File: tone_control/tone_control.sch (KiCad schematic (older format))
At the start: 17 parts, among them J1 filament, J2 B+, J3 audio_in, J4 earth, J5 bass pot (1M), J6 treble pot (250K), J7 audio_out

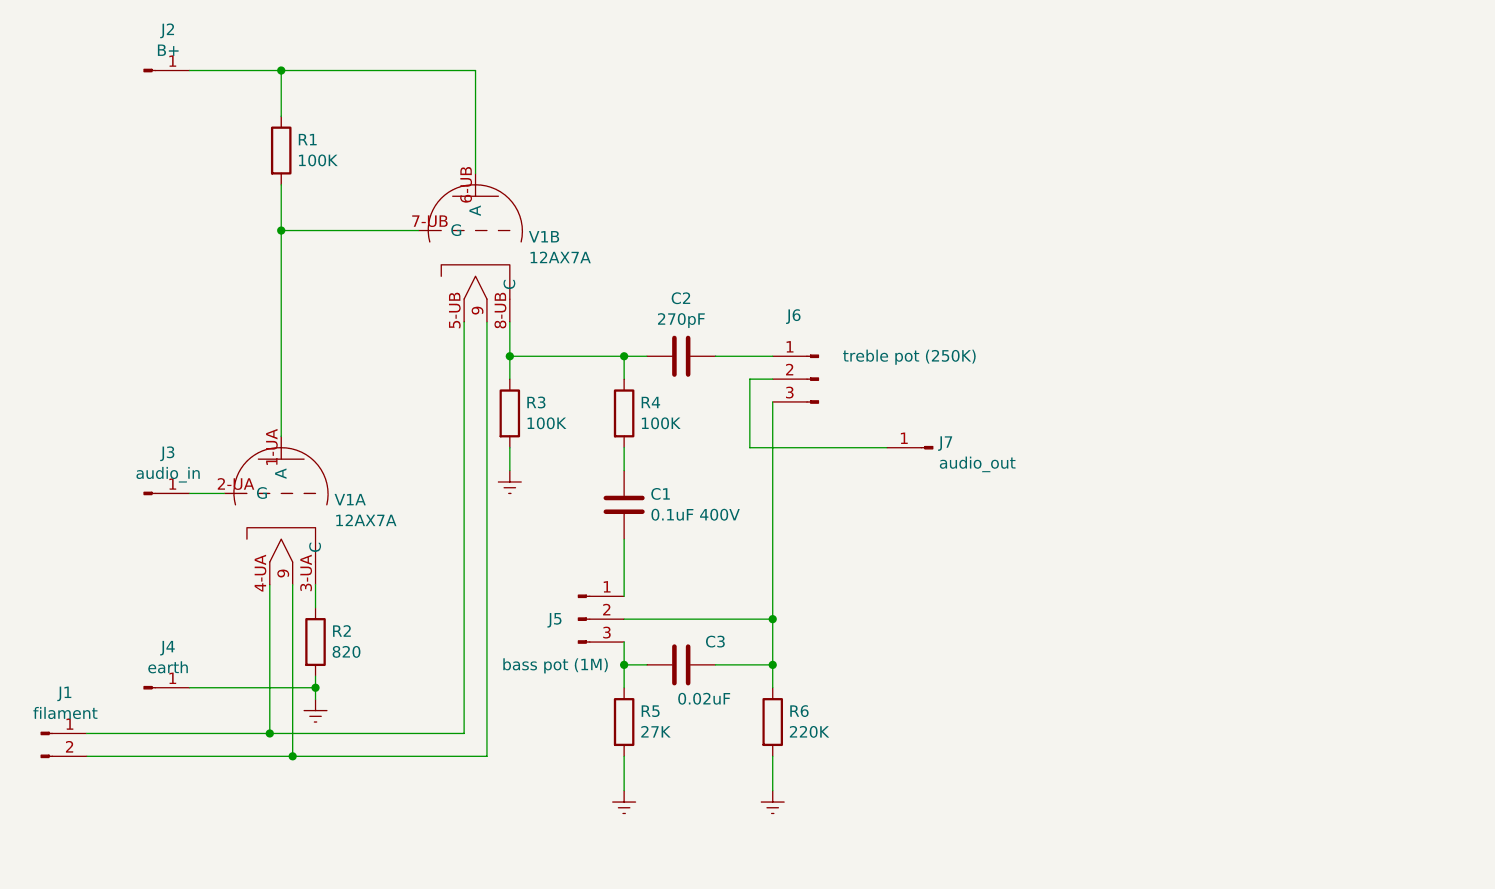
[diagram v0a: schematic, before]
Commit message: refine tone control schematic
some things are chassis mounted
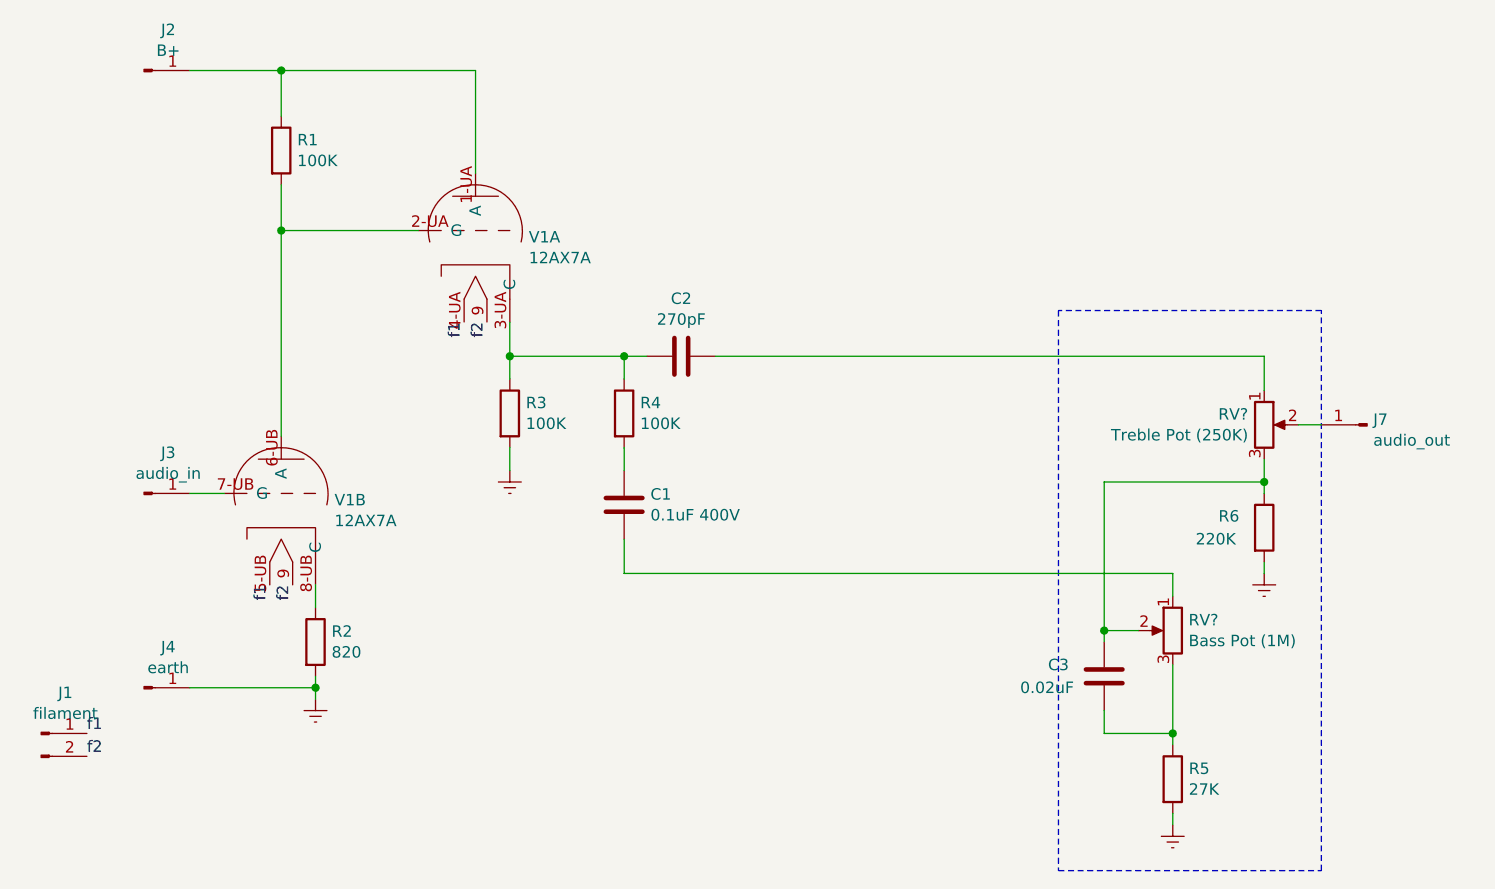
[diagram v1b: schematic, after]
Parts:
- removed J5: bass pot (1M), symbol Connector:Conn_01x03_Male
- removed J6: treble pot (250K), symbol Connector:Conn_01x03_Male
- added RV?: Treble Pot (250K), symbol Device:R_POT
- added RV?: Bass Pot (1M), symbol Device:R_POT
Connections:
- net at J3.1 (Pin_1): now also V1.7-UB (G); no longer V1.2-UA (G)
- net at V1.3-UA (C): now also C2.2, R3.1, R4.1; no longer R2.1
- net f1: now reaches J1.1 (Pin_1), V1.4-UA, V1.5-UB
- net f2: now reaches J1.2 (Pin_2), V1.9, V1.9
- net at J2.1 (Pin_1), R1.1: now also V1.1-UA (A); no longer V1.6-UB (A)
- net at C1.2: now also RV?.1
- net at C2.1: now also RV?.1
- net at J7.1 (Pin_1): now also RV?.2
- net at C3.1, R6.1: now also RV?.2, RV?.3
- net at C3.2, R5.1: now also RV?.3
- new net: R1.2, V1.2-UA (G), V1.6-UB (A)
- new net: R2.1, V1.8-UB (C)
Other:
- moved on the sheet: C3, J7, R5, R6, V1A, V1B
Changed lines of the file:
@@
 EESchema Schematic File Version 4
+LIBS:tone_control-cache
 EELAYER 26 0
 EELAYER END
@@
 L yga1:12AX7A V1
 U 1 1 5C54845C
+P 4900 2050
+F 0 "V1" H 5133 2271 50  0000 L CNN
+F 1 "12AX7A" H 5133 2180 50  0000 L CNN
+F 2 "" H 4900 1700 50  0001 C CNN
+F 3 "" H 4900 1700 50  0001 C CNN
+	1    4900 2050
+	1    0    0    -1
+$EndComp
+$Comp
+L yga1:12AX7A V1
+U 2 1 5C5484C9
 P 4050 3200
 F 0 "V1" H 4283 3421 50  0000 L CNN
@@
 F 2 "" H 4050 2850 50  0001 C CNN
 F 3 "" H 4050 2850 50  0001 C CNN
-	1    4050 3200
-	1    0    0    -1
-$EndComp
-$Comp
-L yga1:12AX7A V1
-U 2 1 5C5484C9
-P 4900 2050
-F 0 "V1" H 5133 2271 50  0000 L CNN
-F 1 "12AX7A" H 5133 2180 50  0000 L CNN
-F 2 "" H 4900 1700 50  0001 C CNN
-F 3 "" H 4900 1700 50  0001 C CNN
-	2    4900 2050
+	2    4050 3200
 	1    0    0    -1
 $EndComp
@@
 	1    0    0    -1
 $EndComp
-Wire Wire Line
-	4000 3350 4000 4000
-Wire Wire Line
-	4000 4000 3200 4000
-Wire Wire Line
-	4100 3350 4100 4100
-Wire Wire Line
-	4100 4100 3200 4100
-Wire Wire Line
-	4100 4100 4950 4100
-Wire Wire Line
-	4950 4100 4950 2200
-Connection ~ 4100 4100
-Wire Wire Line
-	4000 4000 4850 4000
-Wire Wire Line
-	4850 4000 4850 2200
-Connection ~ 4000 4000
 Wire Wire Line
 	4200 3450 4200 3350
@@
 Connection ~ 5550 2350
 $Comp
-L Connector:Conn_01x03_Male J6
-U 1 1 5C54A25B
-P 6400 2450
-F 0 "J6" H 6506 2728 50  0000 C CNN
-F 1 "treble pot (250K)" H 6000 2550 50  0000 C CNN
-F 2 "" H 6400 2450 50  0001 C CNN
-F 3 "~" H 6400 2450 50  0001 C CNN
-	1    6400 2450
-	-1   0    0    -1
-$EndComp
-Wire Wire Line
-	5950 2350 6200 2350
-$Comp
 L Connector:Conn_01x01_Male J7
 U 1 1 5C54A938
-P 6900 2750
-F 0 "J7" H 6873 2773 50  0000 R CNN
-F 1 "audio_out" H 6873 2682 50  0000 R CNN
-F 2 "" H 6900 2750 50  0001 C CNN
-F 3 "~" H 6900 2750 50  0001 C CNN
-	1    6900 2750
+P 8800 2650
+F 0 "J7" H 8773 2673 50  0000 R CNN
+F 1 "audio_out" H 8773 2582 50  0000 R CNN
+F 2 "" H 8800 2650 50  0001 C CNN
+F 3 "~" H 8800 2650 50  0001 C CNN
+	1    8800 2650
 	-1   0    0    -1
 $EndComp
-$Comp
-L Connector:Conn_01x03_Male J5
-U 1 1 5C54AA69
-P 5350 3500
-F 0 "J5" H 5250 3500 50  0000 C CNN
-F 1 "bass pot (1M)" H 5250 3300 50  0000 C CNN
-F 2 "" H 5350 3500 50  0001 C CNN
-F 3 "~" H 5350 3500 50  0001 C CNN
-	1    5350 3500
-	1    0    0    -1
-$EndComp
-Wire Wire Line
-	5550 3150 5550 3400
+Wire Wire Line
+	5550 3150 5550 3300
 $Comp
 L Device:R R5
 U 1 1 5C54AE63
-P 5550 3950
-F 0 "R5" H 5620 3996 50  0000 L CNN
-F 1 "27K" H 5620 3905 50  0000 L CNN
-F 2 "" V 5480 3950 50  0001 C CNN
-F 3 "~" H 5550 3950 50  0001 C CNN
-	1    5550 3950
-	1    0    0    -1
-$EndComp
-Wire Wire Line
-	5550 3600 5550 3700
-$Comp
-L power:Earth #PWR03
-U 1 1 5C54B1C4
-P 5550 4250
-F 0 "#PWR03" H 5550 4000 50  0001 C CNN
-F 1 "Earth" H 5550 4100 50  0001 C CNN
-F 2 "" H 5550 4250 50  0001 C CNN
-F 3 "~" H 5550 4250 50  0001 C CNN
-	1    5550 4250
-	1    0    0    -1
-$EndComp
-Wire Wire Line
-	5550 4100 5550 4250
+P 7950 4200
+F 0 "R5" H 8020 4246 50  0000 L CNN
+F 1 "27K" H 8020 4155 50  0000 L CNN
+F 2 "" V 7880 4200 50  0001 C CNN
+F 3 "~" H 7950 4200 50  0001 C CNN
+	1    7950 4200
+	1    0    0    -1
+$EndComp
 $Comp
 L Device:C C3
 U 1 1 5C54B510
-P 5800 3700
-F 0 "C3" V 5700 3850 50  0000 C CNN
-F 1 "0.02uF" V 5950 3800 50  0000 C CNN
-F 2 "" H 5838 3550 50  0001 C CNN
-F 3 "~" H 5800 3700 50  0001 C CNN
-	1    5800 3700
-	0    1    1    0
-$EndComp
-Wire Wire Line
-	5650 3700 5550 3700
-Connection ~ 5550 3700
-Wire Wire Line
-	5550 3700 5550 3800
-Wire Wire Line
-	6200 2550 6200 3500
-Wire Wire Line
-	6200 3500 5550 3500
-Wire Wire Line
-	6200 3500 6200 3700
-Wire Wire Line
-	6200 3700 5950 3700
-Connection ~ 6200 3500
+P 7650 3750
+F 0 "C3" H 7450 3800 50  0000 C CNN
+F 1 "0.02uF" H 7400 3700 50  0000 C CNN
+F 2 "" H 7688 3600 50  0001 C CNN
+F 3 "~" H 7650 3750 50  0001 C CNN
+	1    7650 3750
+	1    0    0    -1
+$EndComp
 $Comp
 L Device:R R6
 U 1 1 5C54C0D0
-P 6200 3950
-F 0 "R6" H 6270 3996 50  0000 L CNN
-F 1 "220K" H 6270 3905 50  0000 L CNN
-F 2 "" V 6130 3950 50  0001 C CNN
-F 3 "~" H 6200 3950 50  0001 C CNN
-	1    6200 3950
-	1    0    0    -1
-$EndComp
-$Comp
-L power:Earth #PWR04
-U 1 1 5C54C54E
-P 6200 4250
-F 0 "#PWR04" H 6200 4000 50  0001 C CNN
-F 1 "Earth" H 6200 4100 50  0001 C CNN
-F 2 "" H 6200 4250 50  0001 C CNN
-F 3 "~" H 6200 4250 50  0001 C CNN
-	1    6200 4250
-	1    0    0    -1
-$EndComp
-Wire Wire Line
-	6200 4100 6200 4250
-Wire Wire Line
-	6200 3700 6200 3800
-Connection ~ 6200 3700
-Wire Wire Line
-	6200 2450 6100 2450
-Wire Wire Line
-	6100 2450 6100 2750
-Wire Wire Line
-	6100 2750 6700 2750
+P 8350 3100
+F 0 "R6" H 8150 3150 50  0000 L CNN
+F 1 "220K" H 8050 3050 50  0000 L CNN
+F 2 "" V 8280 3100 50  0001 C CNN
+F 3 "~" H 8350 3100 50  0001 C CNN
+	1    8350 3100
+	1    0    0    -1
+$EndComp
 $Comp
 L Connector:Conn_01x01_Male J4
@@
 Wire Wire Line
 	4200 3800 4200 3850
+Text Label 3200 4000 0    50   ~ 0
+f1
+Text Label 3200 4100 0    50   ~ 0
+f2
+Text Label 4850 2200 3    50   ~ 0
+f1
+Text Label 4950 2200 3    50   ~ 0
+f2
+Text Label 4000 3350 3    50   ~ 0
+f1
+Text Label 4100 3350 3    50   ~ 0
+f2
+$Comp
+L Device:R_POT RV?
+U 1 1 5C561307
+P 8350 2650
+F 0 "RV?" H 8280 2696 50  0000 R CNN
+F 1 "Treble Pot (250K)" H 8280 2605 50  0000 R CNN
+F 2 "" H 8350 2650 50  0001 C CNN
+F 3 "~" H 8350 2650 50  0001 C CNN
+	1    8350 2650
+	1    0    0    -1
+$EndComp
+$Comp
+L power:Earth #PWR?
+U 1 1 5C561842
+P 8350 3300
+F 0 "#PWR?" H 8350 3050 50  0001 C CNN
+F 1 "Earth" H 8350 3150 50  0001 C CNN
+F 2 "" H 8350 3300 50  0001 C CNN
+F 3 "~" H 8350 3300 50  0001 C CNN
+	1    8350 3300
+	1    0    0    -1
+$EndComp
+$Comp
+L Device:R_POT RV?
+U 1 1 5C563429
+P 7950 3550
+F 0 "RV?" H 7881 3596 50  0000 R CNN
+F 1 "Bass Pot (1M)" H 7881 3505 50  0000 R CNN
+F 2 "" H 7950 3550 50  0001 C CNN
+F 3 "~" H 7950 3550 50  0001 C CNN
+	1    7950 3550
+	-1   0    0    -1
+$EndComp
+Wire Wire Line
+	7650 3600 7650 3550
+Wire Wire Line
+	7650 3550 7800 3550
+Wire Wire Line
+	7650 3900 7650 4000
+Wire Wire Line
+	7650 4000 7950 4000
+Wire Wire Line
+	7950 4000 7950 3700
+Wire Wire Line
+	7950 4050 7950 4000
+Connection ~ 7950 4000
+$Comp
+L power:Earth #PWR?
+U 1 1 5C567F52
+P 7950 4400
+F 0 "#PWR?" H 7950 4150 50  0001 C CNN
+F 1 "Earth" H 7950 4250 50  0001 C CNN
+F 2 "" H 7950 4400 50  0001 C CNN
+F 3 "~" H 7950 4400 50  0001 C CNN
+	1    7950 4400
+	1    0    0    -1
+$EndComp
+Wire Wire Line
+	7950 4400 7950 4350
+Wire Wire Line
+	8350 3300 8350 3250
+Wire Wire Line
+	8350 2800 8350 2900
+Wire Wire Line
+	8350 2900 7650 2900
+Connection ~ 8350 2900
+Wire Wire Line
+	8350 2900 8350 2950
+Connection ~ 7650 3550
+Wire Wire Line
+	7950 3400 7950 3300
+Wire Wire Line
+	7950 3300 5550 3300
+Wire Wire Line
+	7650 2900 7650 3550
+Wire Wire Line
+	8350 2350 8350 2500
+Wire Wire Line
+	5950 2350 8350 2350
+Wire Wire Line
+	8600 2650 8500 2650
+Wire Notes Line
+	7450 4600 8600 4600
+Wire Notes Line
+	8600 4600 8600 2150
+Wire Notes Line
+	8600 2150 7450 2150
+Wire Notes Line
+	7450 2150 7450 4600
 $EndSCHEMATC
